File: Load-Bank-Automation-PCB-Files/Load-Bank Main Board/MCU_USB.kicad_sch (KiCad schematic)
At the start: 23 parts, among them J26 STM32-Prog-Header, SW2 SW_SPDT, SW4 RESET, U13 STM32G491VETx, U2 OXETDLJANF-8MHz

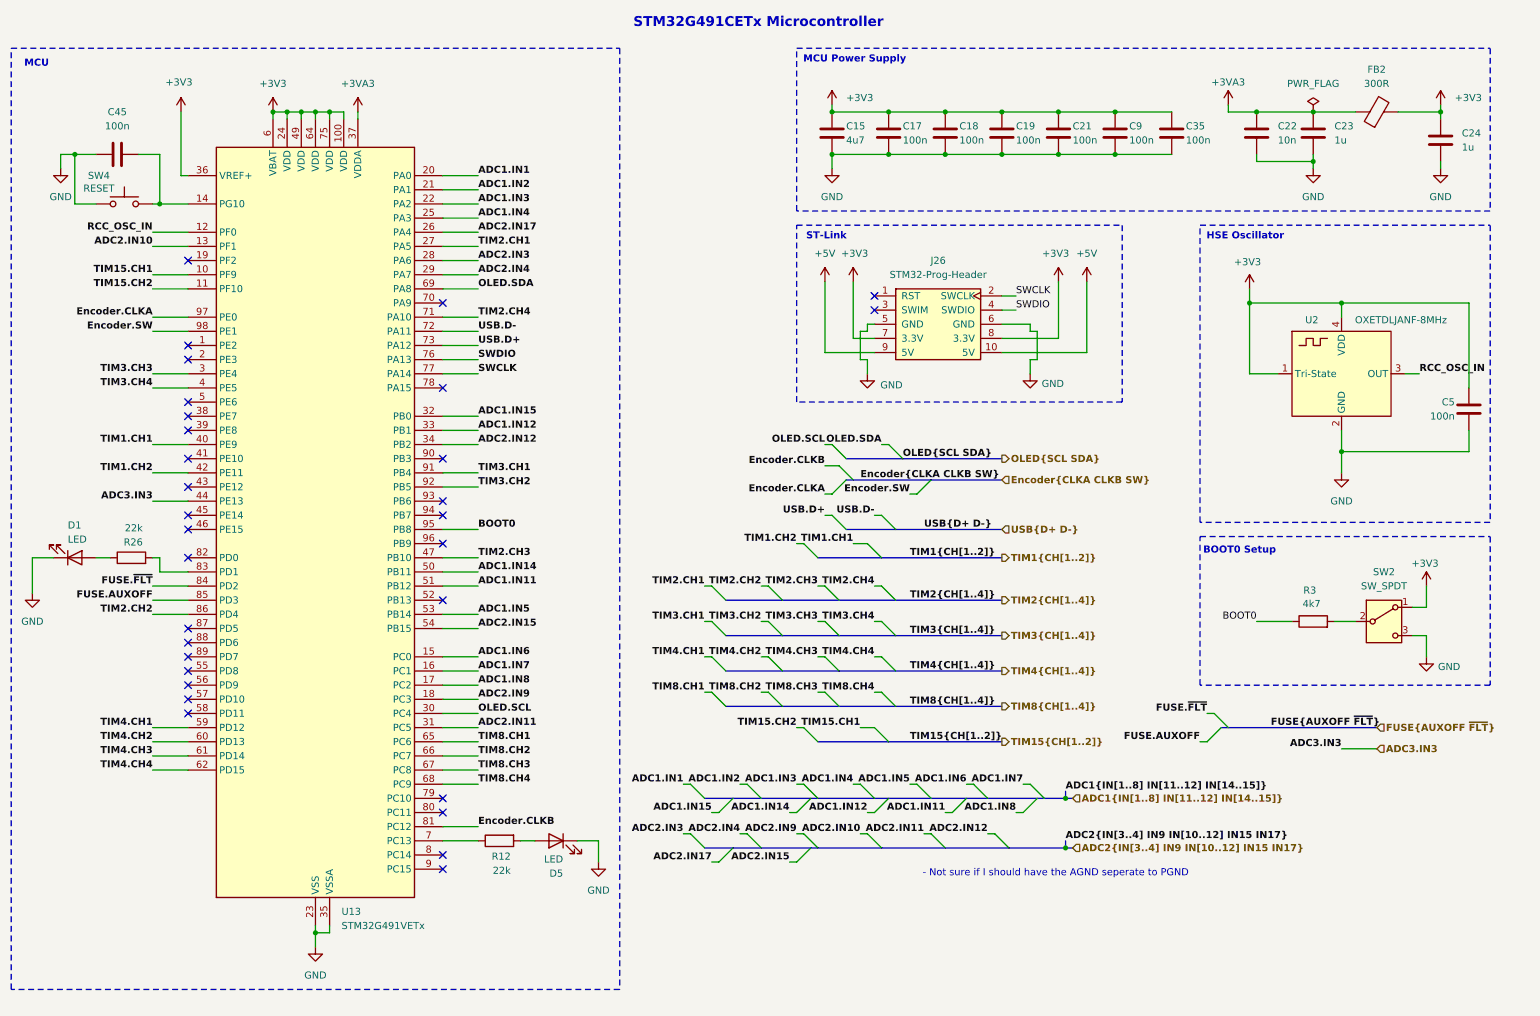
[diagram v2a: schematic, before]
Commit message: Replaced 12V-5V LDO with buck
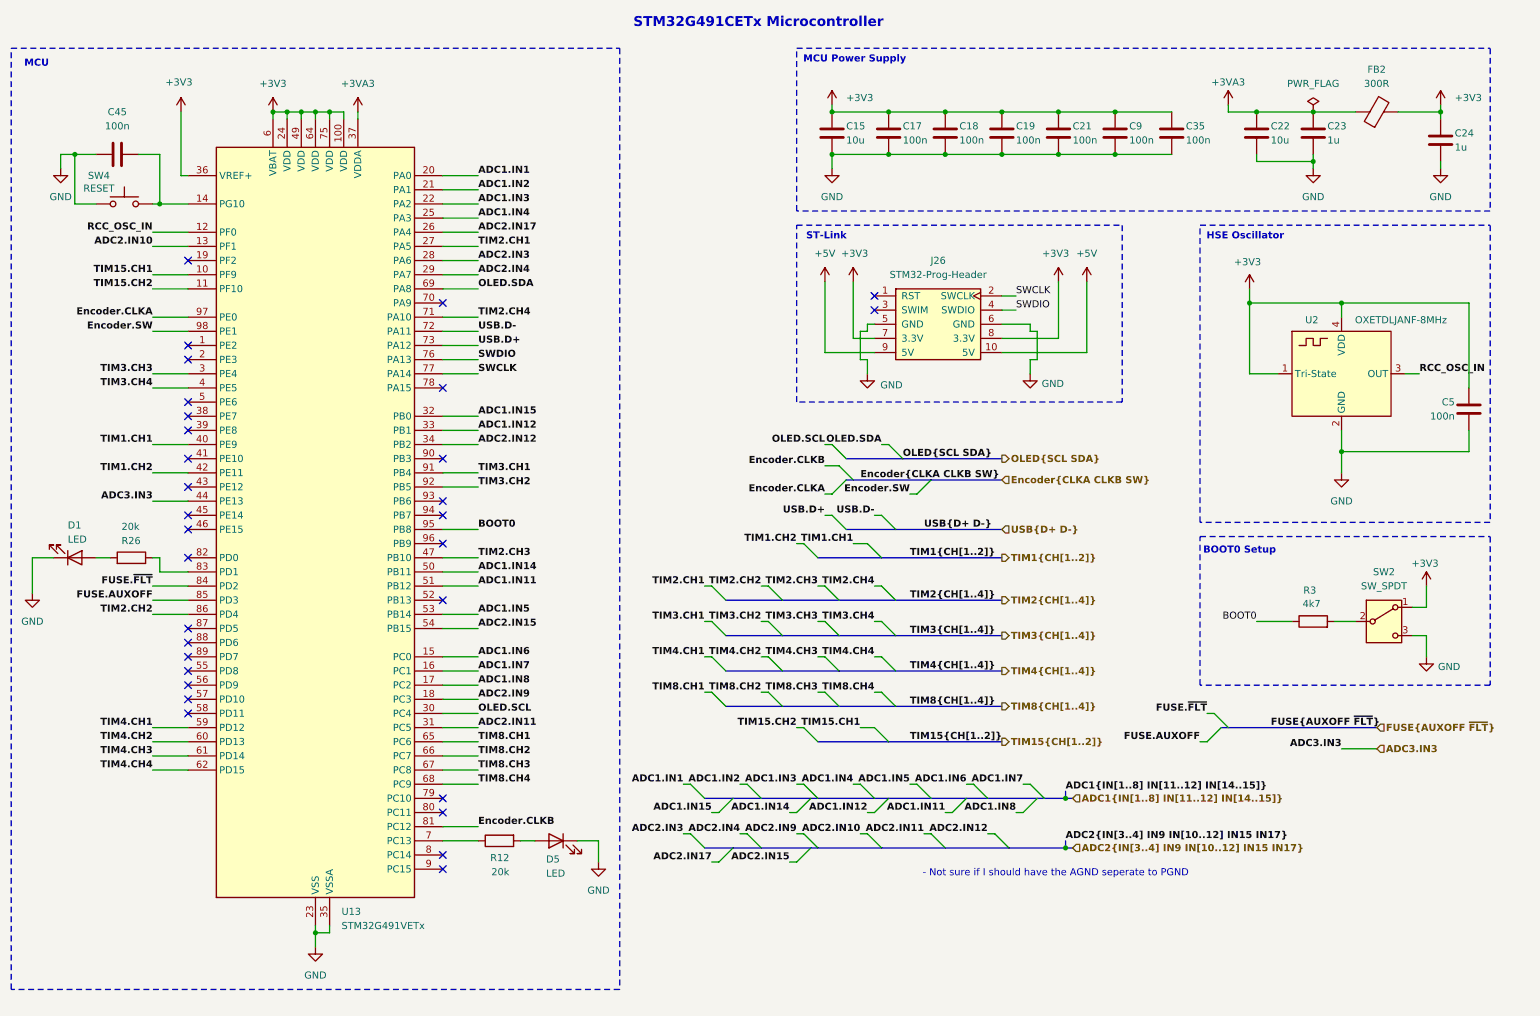
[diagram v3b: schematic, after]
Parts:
- C15: value 4u7 -> 10u
- C17: footprint Capacitor_SMD:C_1206_3216Metric_Pad1.33x1.80mm_HandSolder -> Capacitor_SMD:C_0805_2012Metric_Pad1.18x1.45mm_HandSolder
- C22: value 10n -> 10u; footprint Capacitor_SMD:C_0402_1005Metric_Pad0.74x0.62mm_HandSolder -> Capacitor_SMD:C_1206_3216Metric_Pad1.33x1.80mm_HandSolder
- C23, C24: footprint Capacitor_SMD:C_0402_1005Metric_Pad0.74x0.62mm_HandSolder -> Capacitor_SMD:C_1206_3216Metric_Pad1.33x1.80mm_HandSolder
- R12, R26: value 22k -> 20k; footprint Resistor_SMD:R_1206_3216Metric_Pad1.30x1.75mm_HandSolder -> Resistor_SMD:R_0603_1608Metric_Pad0.98x0.95mm_HandSolder
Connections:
- net at U13.83 (PD1): now also R26.1; no longer R26.2
- net at D1.2 (A): now also R26.2; no longer R26.1

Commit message: A
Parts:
- removed C21, C45: 100n, Capacitor_SMD:C_1206_3216Metric_Pad1.33x1.80mm_HandSolder, symbol Device:C
- added C7, C8: 100n, Capacitor_SMD:C_0603_1608Metric_Pad1.08x0.95mm_HandSolder, symbol Device:C
- C17: footprint Capacitor_SMD:C_0805_2012Metric_Pad1.18x1.45mm_HandSolder -> Capacitor_SMD:C_0603_1608Metric_Pad1.08x0.95mm_HandSolder
- C18, C19, C35, C5, C9: footprint Capacitor_SMD:C_1206_3216Metric_Pad1.33x1.80mm_HandSolder -> Capacitor_SMD:C_0603_1608Metric_Pad1.08x0.95mm_HandSolder
- C22: footprint Capacitor_SMD:C_1206_3216Metric_Pad1.33x1.80mm_HandSolder -> Capacitor_SMD:C_0805_2012Metric_Pad1.18x1.45mm_HandSolder
- C23, C24: value 1u -> 100n; footprint Capacitor_SMD:C_1206_3216Metric_Pad1.33x1.80mm_HandSolder -> Capacitor_SMD:C_0603_1608Metric_Pad1.08x0.95mm_HandSolder
- SW4: footprint Button_Switch_SMD:SW_SPST_B3S-1000 -> Button_Switch_THT:SW_PUSH_6mm
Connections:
- net +3V3: now also C7.1, C8.1; no longer C19.1
- net Encoder.CLKA: now also U13.19 (PF2); no longer U13.97 (PE0)
- net Encoder.CLKB: now also U13.2 (PE3); no longer U13.81 (PC12)
- net Encoder.SW: now also U13.1 (PE2); no longer U13.98 (PE1)
- net GND: now also C19.1, C7.2, C8.2; no longer C19.2
- net at SW4.2, U13.14 (PG10): now also C19.2
- net at U13.7 (PC13): no longer R12.1
- net at U13.78 (PA15): now also R26.1
- net at U13.83 (PD1): no longer R26.1
- net at U13.89 (PD7): now also R12.1
- no-connect marks 31 -> 30
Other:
- moved on the sheet: D5, R12

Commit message: A
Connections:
- net FUSE.AUXOFF: no longer names the net of U13.85 (PD3)
- net FUSE.~{FLT}: no longer names the net of U13.84 (PD2)
- no-connect marks 30 -> 33
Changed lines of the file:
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@@
 	)
 	(no_connect
+		(at 49.53 119.38)
+	)
+	(no_connect
 		(at 95.25 101.6)
 	)
@@
 	)
 	(no_connect
+		(at 49.53 71.12)
+	)
+	(no_connect
 		(at 49.53 132.08)
 	)
@@
 	)
 	(no_connect
+		(at 49.53 116.84)
+	)
+	(no_connect
 		(at 49.53 134.62)
 	)
@@
 	)
 	(bus_entry
-		(at 234.95 142.24)
-		(size -2.54 2.54)
-		(stroke
-			(width 0)
-			(type default)
-		)
-	)
-	(bus_entry
 		(at 147.32 154.94)
 		(size -2.54 2.54)
@@
 	)
 	(bus_entry
-		(at 236.22 142.24)
-		(size -2.54 -2.54)
-		(stroke
-			(width 0)
-			(type default)
-		)
-	)
-	(bus_entry
 		(at 173.99 111.76)
 		(size -2.54 -2.54)
@@
 	(wire
 		(pts
-			(xy 43.18 119.38) (xy 49.53 119.38)
-		)
-		(stroke
-			(width 0)
-			(type default)
-		)
-	)
-	(wire
-		(pts
 			(xy 95.25 129.54) (xy 101.6 129.54)
 		)
@@
 	(wire
 		(pts
-			(xy 232.41 144.78) (xy 231.14 144.78)
-		)
-		(stroke
-			(width 0)
-			(type default)
-		)
-	)
-	(wire
-		(pts
 			(xy 95.25 99.06) (xy 101.6 99.06)
 		)
@@
 	(wire
 		(pts
-			(xy 43.18 116.84) (xy 49.53 116.84)
-		)
-		(stroke
-			(width 0)
-			(type default)
-		)
-	)
-	(wire
-		(pts
 			(xy 95.25 134.62) (xy 101.6 134.62)
 		)
@@
 		)
 	)
-	(bus
-		(pts
-			(xy 236.22 142.24) (xy 262.89 142.24)
-		)
-		(stroke
-			(width 0)
-			(type default)
-		)
-	)
 	(wire
 		(pts
@@
 		)
 	)
-	(bus
-		(pts
-			(xy 234.95 142.24) (xy 236.22 142.24)
-		)
-		(stroke
-			(width 0)
-			(type default)
-		)
-	)
 	(wire
 		(pts
@@
 	(wire
 		(pts
-			(xy 262.89 146.05) (xy 256.54 146.05)
+			(xy 262.89 139.7) (xy 256.54 139.7)
 		)
 		(stroke
@@
 	(wire
 		(pts
-			(xy 233.68 139.7) (xy 232.41 139.7)
-		)
-		(stroke
-			(width 0)
-			(type default)
-		)
-	)
-	(wire
-		(pts
 			(xy 279.4 66.04) (xy 256.54 66.04)
 		)
@@
 		)
 	)
-	(label "FUSE.~{FLT}"
-		(at 232.41 139.7 180)
-		(effects
-			(font
-				(size 1.27 1.27)
-				(thickness 0.254)
-				(bold yes)
-			)
-			(justify right bottom)
-		)
-	)
 	(label "ADC2.IN11"
 		(at 181.61 161.29 180)
@@
 	)
 	(label "ADC3.IN3"
-		(at 256.54 146.05 180)
+		(at 256.54 139.7 180)
 		(effects
 			(font
@@
 		)
 	)
-	(label "FUSE.AUXOFF"
-		(at 231.14 144.78 180)
-		(effects
-			(font
-				(size 1.27 1.27)
-				(thickness 0.254)
-				(bold yes)
-			)
-			(justify right bottom)
-		)
-	)
 	(label "ADC1.IN6"
 		(at 189.23 152.4 180)
@@
 		)
 	)
-	(label "FUSE{AUXOFF ~{FLT}}"
-		(at 243.84 142.24 0)
-		(effects
-			(font
-				(size 1.27 1.27)
-				(thickness 0.254)
-				(bold yes)
-			)
-			(justify left bottom)
-		)
-	)
 	(label "ADC2{IN[3..4] IN9 IN[10..12] IN15 IN17}"
 		(at 207.01 162.56 0)
@@
 		)
 	)
-	(label "FUSE.AUXOFF"
-		(at 43.18 119.38 180)
-		(effects
-			(font
-				(size 1.27 1.27)
-				(thickness 0.254)
-				(bold yes)
-			)
-			(justify right bottom)
-		)
-	)
 	(label "ADC1.IN5"
 		(at 101.6 121.92 0)
@@
 		)
 	)
-	(label "FUSE.~{FLT}"
-		(at 43.18 116.84 180)
-		(effects
-			(font
-				(size 1.27 1.27)
-				(thickness 0.254)
-				(bold yes)
-			)
-			(justify right bottom)
-		)
-	)
 	(label "Encoder{CLKA CLKB SW}"
 		(at 170.18 97.79 0)
@@
 	(hierarchical_label "ADC3.IN3"
 		(shape input)
-		(at 262.89 146.05 0)
+		(at 262.89 139.7 0)
 		(effects
 			(font
@@
 		(effects
 			(font
-				(size 1.27 1.27)
-				(thickness 0.254)
-				(bold yes)
-			)
-			(justify left)
-		)
-	)
-	(hierarchical_label "FUSE{AUXOFF ~{FLT}}"
-		(shape input)
-		(at 262.89 142.24 0)
-		(effects
-			(font

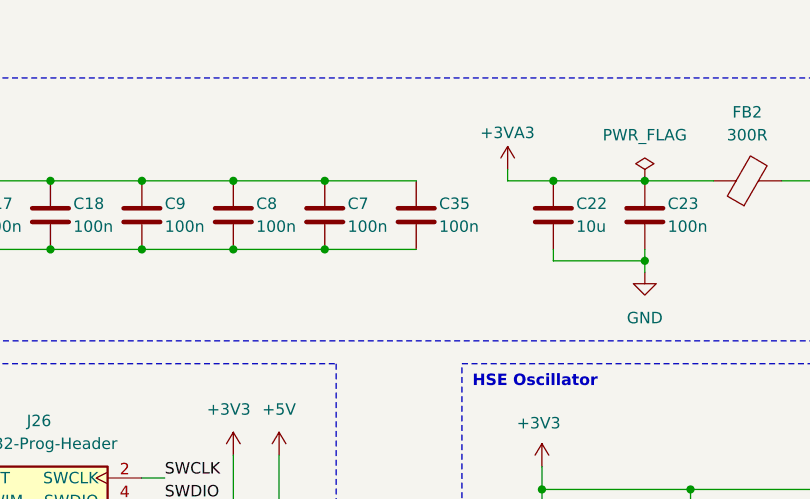
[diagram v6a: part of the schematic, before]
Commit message: Layout Placement Complete, Routing Remains
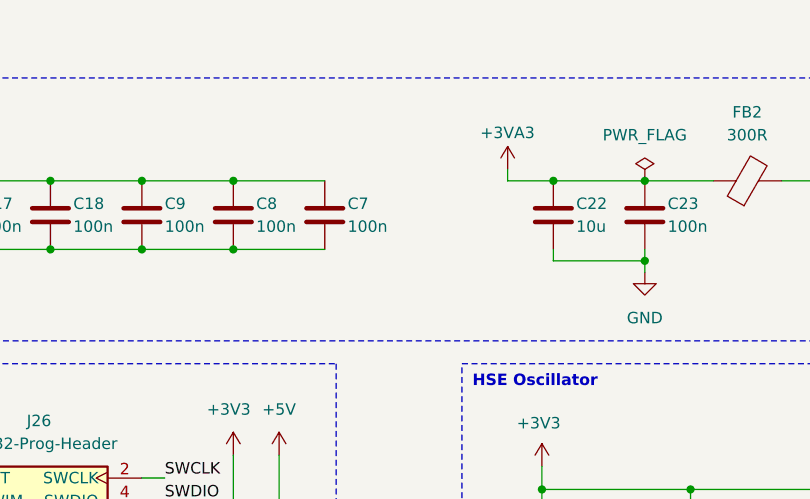
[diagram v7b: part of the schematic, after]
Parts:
- removed C35: 100n, Capacitor_SMD:C_0603_1608Metric_Pad1.08x0.95mm_HandSolder, symbol Device:C
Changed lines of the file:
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@@
 	)
 	(junction
-		(at 215.9 39.37)
-		(diameter 0)
-		(color 0 0 0 0)
-	)
-	(junction
 		(at 251.46 31.75)
 		(diameter 0)
@@
 	)
 	(junction
-		(at 215.9 31.75)
-		(diameter 0)
-		(color 0 0 0 0)
-	)
-	(junction
 		(at 241.3 31.75)
 		(diameter 0)
@@
 	(wire
 		(pts
-			(xy 215.9 39.37) (xy 226.06 39.37)
-		)
-		(stroke
-			(width 0)
-			(type default)
-		)
-	)
-	(wire
-		(pts
 			(xy 95.25 55.88) (xy 101.6 55.88)
 		)
@@
 	(wire
 		(pts
-			(xy 215.9 31.75) (xy 226.06 31.75)
-		)
-		(stroke
-			(width 0)
-			(type default)
-		)
-	)
-	(wire
-		(pts
 			(xy 72.39 181.61) (xy 72.39 179.07)
 		)
@@
 					(unit 1)
 				)
-			)
-		)
-	)
-	(symbol
-		(lib_id "Device:C")
-		(at 226.06 35.56 0)
-		(unit 1)
-		(exclude_from_sim no)
-		(in_bom yes)
-		(on_board yes)
-		(dnp no)
-		(property "Reference" "C35"
-			(at 228.6 34.29 0)
-			(effects
-				(font
-					(size 1.27 1.27)
-				)
-				(justify left)
-			)
-		)
-		(property "Value" "100n"
-			(at 228.6 36.83 0)
-			(effects
-				(font
-					(size 1.27 1.27)
-				)
-				(justify left)
-			)
-		)
-		(property "Footprint" "Capacitor_SMD:C_0603_1608Metric_Pad1.08x0.95mm_HandSolder"
-			(at 227.0252 39.37 0)
-			(effects
-				(font
-					(size 1.27 1.27)
-				)
-				(hide yes)
-			)
-		)
-		(property "Datasheet" "https://www.digikey.ca/en/products/detail/tdk-corporation/CGA3E2X7R1H104K080AA/2443144?s=N4IgTCBcDaIDoBcAEBhA4gQQMwFEwA0B2AJQEYAJUgBgBYBpKgDiowxAF0BfIA"
-			(at 226.06 35.56 0)
-			(effects
-				(font
-					(size 1.27 1.27)
-				)
-				(hide yes)
-			)
-		)
-		(property "Description" "Unpolarized capacitor"
-			(at 226.06 35.56 0)
-			(effects
-				(font
-					(size 1.27 1.27)
-				)
-				(hide yes)
-			)
-		)
-		(pin "1"
-		)
-		(pin "2"
-		)
-		(instances
-			(project "Main Board"
-				(path "/c82c4769-33eb-46b7-8d07-39045014a3da/a4307ae8-dc68-4212-b4d2-d8b3b6e70043"
-					(reference "C35")
-					(unit 1)
-				)

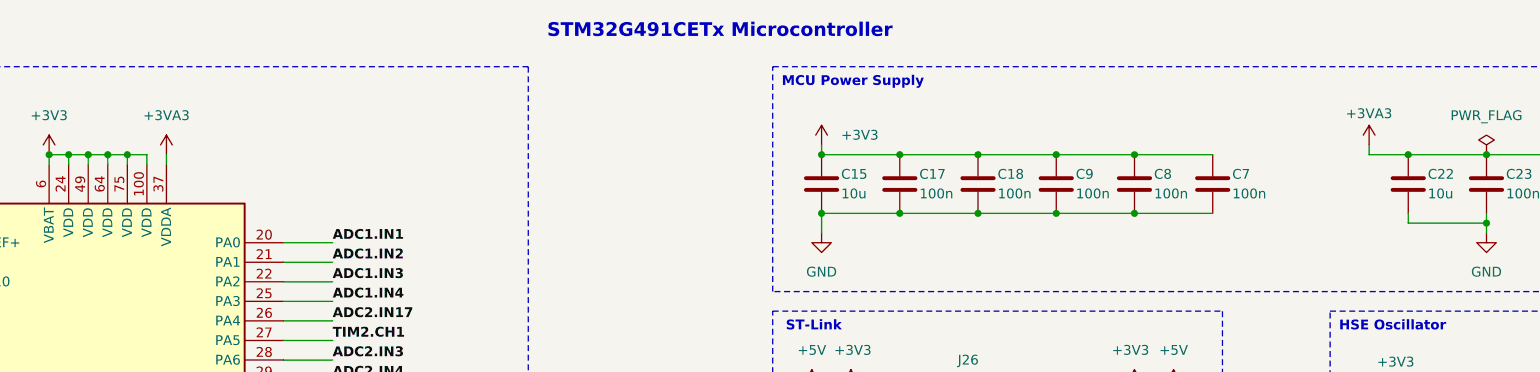
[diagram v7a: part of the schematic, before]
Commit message: All Digital Circuitry Connected
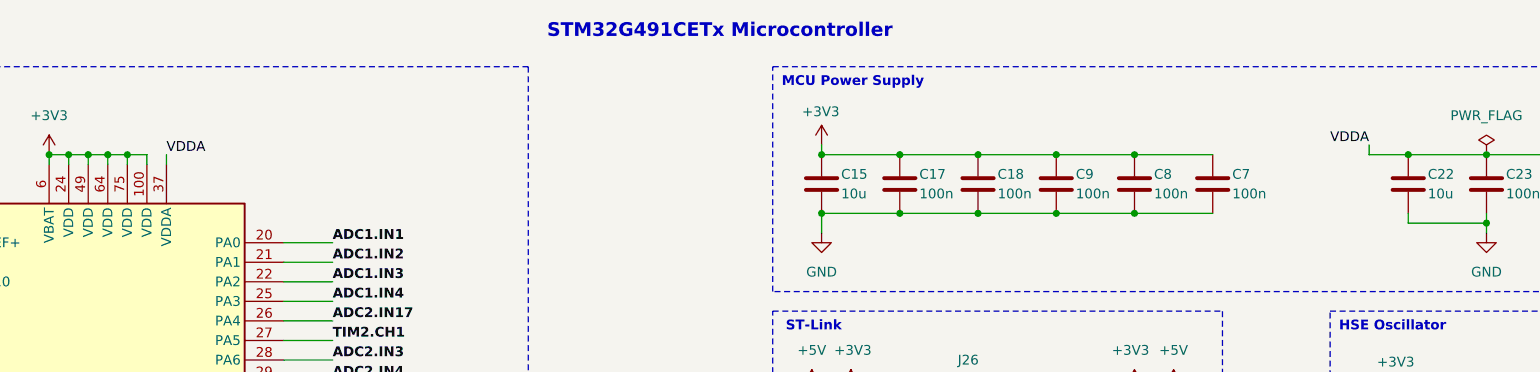
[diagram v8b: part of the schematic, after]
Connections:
- net +3VA3 renamed VDDA
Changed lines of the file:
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@@
 		)
 	)
+	(label "VDDA"
+		(at 80.01 31.75 0)
+		(effects
+			(font
+				(size 1.27 1.27)
+			)
+			(justify left bottom)
+		)
+	)
 	(label "ADC2{IN[3..4] IN9 IN[10..12] IN15 IN17}"
 		(at 207.01 162.56 0)
@@
 		)
 	)
+	(label "VDDA"
+		(at 236.22 30.48 180)
+		(effects
+			(font
+				(size 1.27 1.27)
+			)
+			(justify right bottom)
+		)
+	)
 	(label "TIM4.CH2"
 		(at 43.18 144.78 180)
@@
 		(on_board yes)
 		(dnp no)
-		(fields_autoplaced yes)
 		(property "Reference" "#PWR027"
 			(at 165.1 34.29 0)
@@
 		)
 		(property "Value" "+3V3"
-			(at 167.64 29.2099 0)
+			(at 162.56 26.162 0)
 			(effects
 				(font
@@
 	)
 	(symbol
-		(lib_id "power:+3.3VA")
-		(at 80.01 31.75 0)
-		(unit 1)
-		(exclude_from_sim no)
-		(in_bom yes)
-		(on_board yes)
-		(dnp no)
-		(property "Reference" "#PWR082"
-			(at 80.01 35.56 0)
-			(effects
-				(font
-					(size 1.27 1.27)
-				)
-				(hide yes)
-			)
-		)
-		(property "Value" "+3VA3"
-			(at 80.01 26.67 0)
-			(effects
-				(font
-					(size 1.27 1.27)
-				)
-			)
-		)
-		(property "Footprint" ""
-			(at 80.01 31.75 0)
-			(effects
-				(font
-					(size 1.27 1.27)
-				)
-				(hide yes)
-			)
-		)
-		(property "Datasheet" ""
-			(at 80.01 31.75 0)
-			(effects
-				(font
-					(size 1.27 1.27)
-				)
-				(hide yes)
-			)
-		)
-		(property "Description" "Power symbol creates a global label with name \"+3.3VA\""
-			(at 80.01 31.75 0)
-			(effects
-				(font
-					(size 1.27 1.27)
-				)
-				(hide yes)
-			)
-		)
-		(pin "1"
-		)
-		(instances
-			(project "Main Board"
-				(path "/c82c4769-33eb-46b7-8d07-39045014a3da/a4307ae8-dc68-4212-b4d2-d8b3b6e70043"
-					(reference "#PWR082")
-					(unit 1)
-				)
-			)
-		)
-	)
-	(symbol
 		(lib_id "power:GND")
 		(at 26.67 41.91 0)
@@
 					(unit 1)
 				)
-			)
-		)
-	)
-	(symbol
-		(lib_id "power:+3.3VA")
-		(at 236.22 30.48 0)
-		(unit 1)
-		(exclude_from_sim no)
-		(in_bom yes)
-		(on_board yes)
-		(dnp no)
-		(property "Reference" "#PWR030"
-			(at 236.22 34.29 0)
-			(effects
-				(font
-					(size 1.27 1.27)
-				)
-				(hide yes)
-			)
-		)
-		(property "Value" "+3VA3"
-			(at 233.172 26.416 0)
-			(effects
-				(font
-					(size 1.27 1.27)
-				)
-				(justify left)
-			)
-		)
-		(property "Footprint" ""
-			(at 236.22 30.48 0)
-			(effects
-				(font
-					(size 1.27 1.27)
-				)
-				(hide yes)
-			)
-		)
-		(property "Datasheet" ""
-			(at 236.22 30.48 0)
-			(effects
-				(font
-					(size 1.27 1.27)
-				)
-				(hide yes)
-			)
-		)
-		(property "Description" "Power symbol creates a global label with name \"+3.3VA\""
-			(at 236.22 30.48 0)
-			(effects
-				(font
-					(size 1.27 1.27)
-				)
-				(hide yes)
-			)
-		)
-		(pin "1"
-		)
-		(instances
-			(project "Main Board"
-				(path "/c82c4769-33eb-46b7-8d07-39045014a3da/a4307ae8-dc68-4212-b4d2-d8b3b6e70043"
-					(reference "#PWR030")
-					(unit 1)
-				)
